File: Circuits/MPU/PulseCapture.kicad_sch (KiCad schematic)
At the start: 12 parts, among them U15 AD7984BRMZ, U18 LT1715

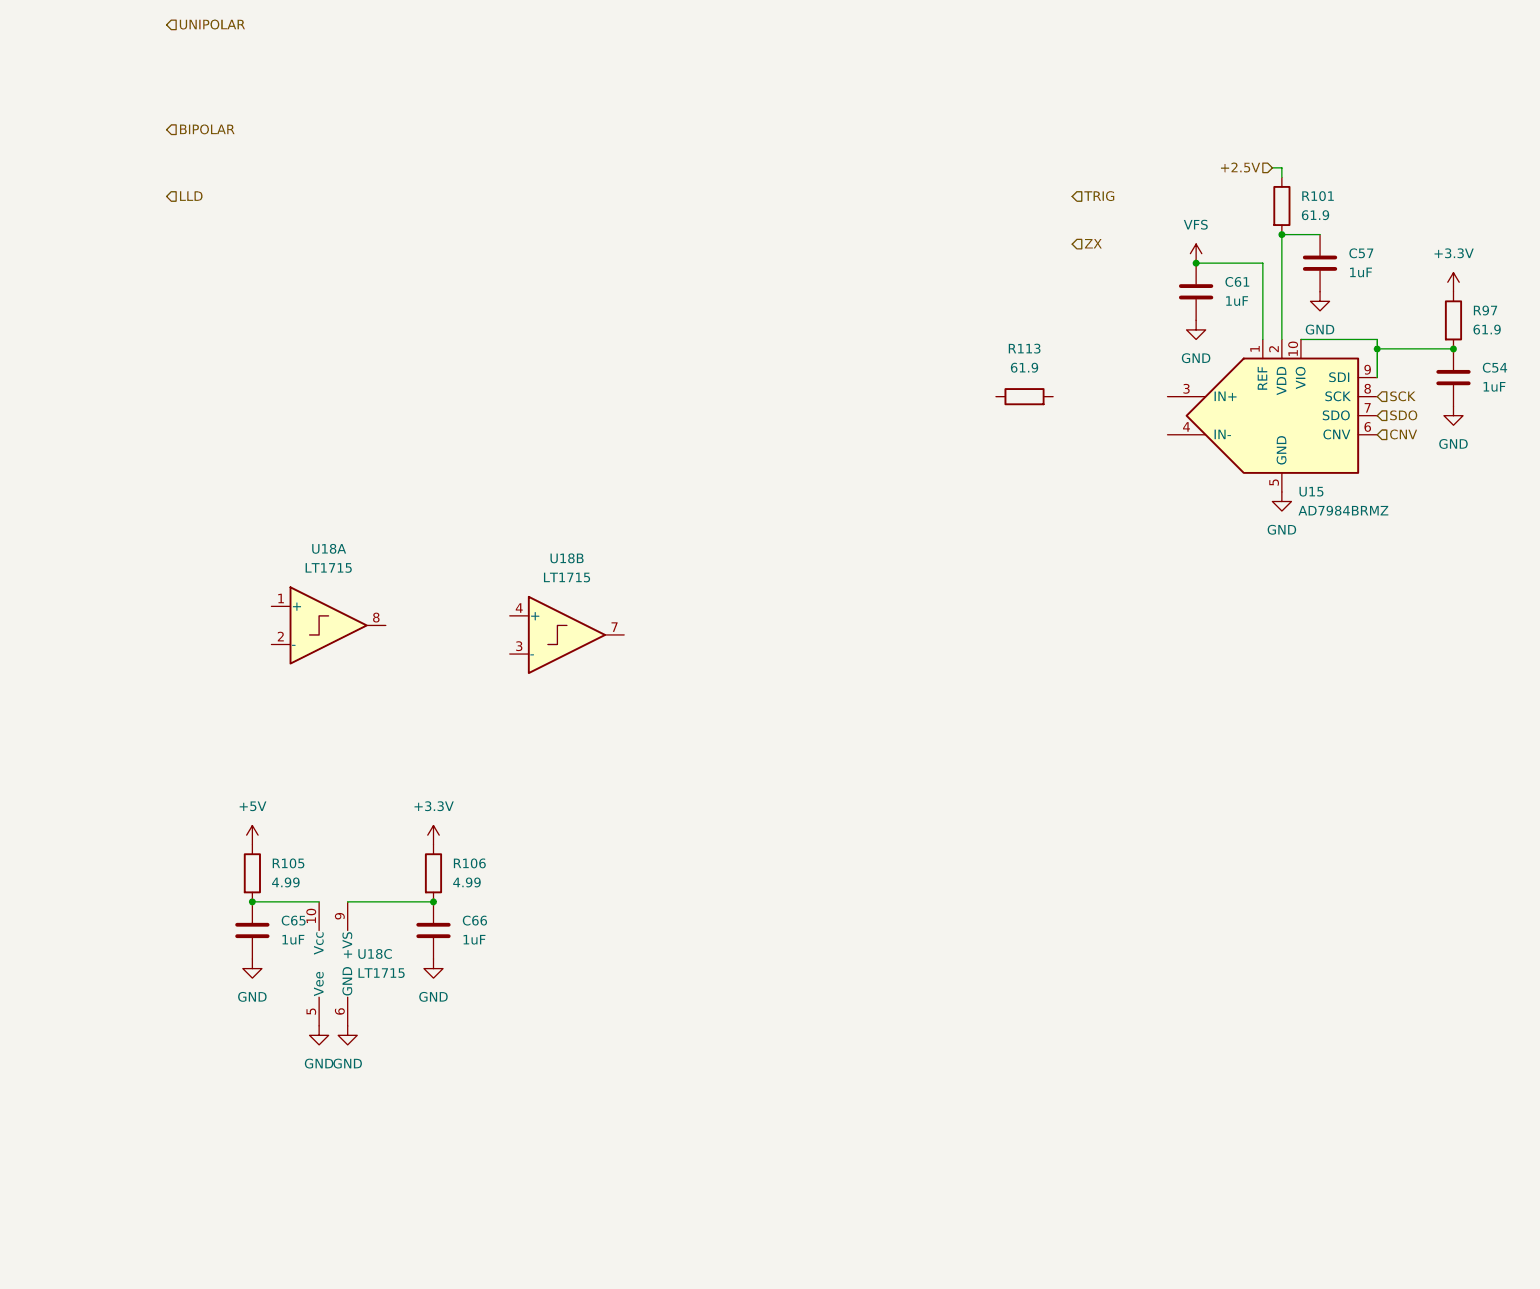
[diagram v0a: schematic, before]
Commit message: All pages populated with parts
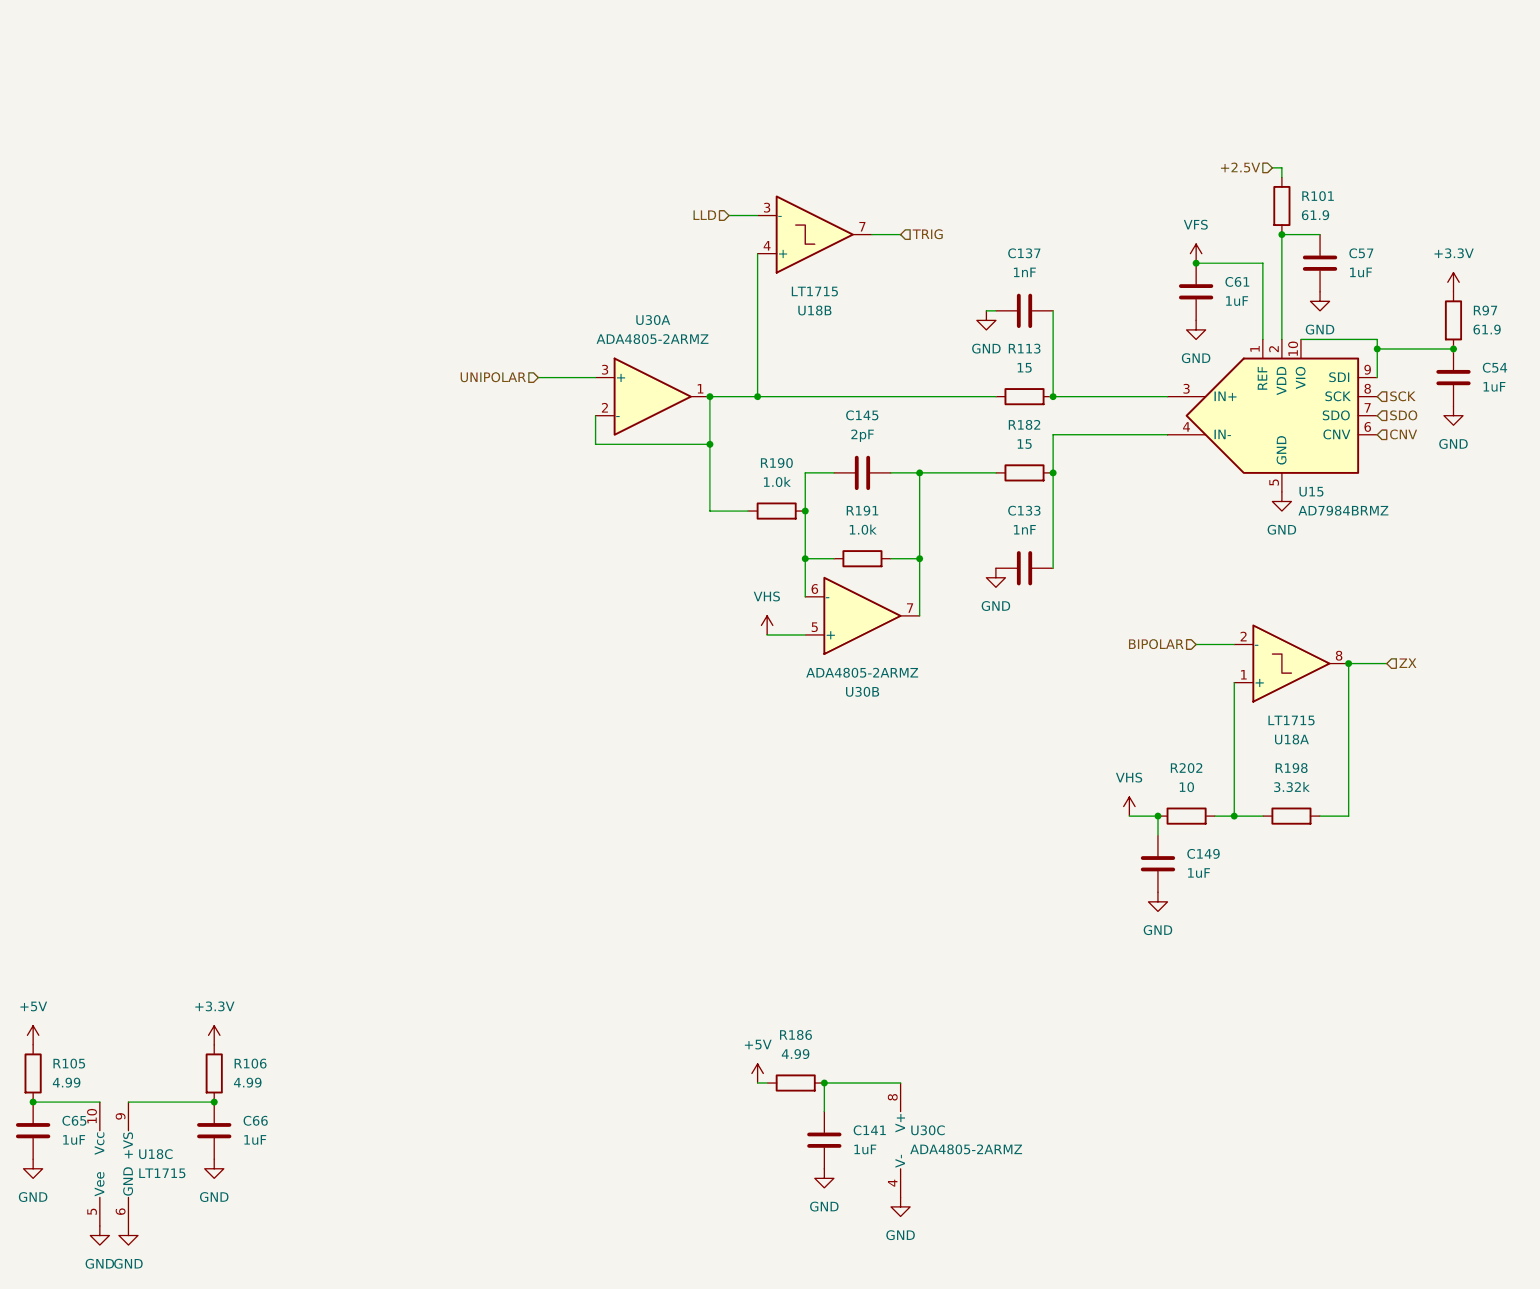
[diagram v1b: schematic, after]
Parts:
- added C133, C137: 1nF, Capacitor_SMD:C_0603_1608Metric, symbol QuERI_symbols:Csmall
- added C141, C149: 1uF, Capacitor_SMD:C_0805_2012Metric, symbol QuERI_symbols:C
- added C145: 2pF, Capacitor_SMD:C_0603_1608Metric, symbol QuERI_symbols:Csmall
- added R182: 15, Resistor_SMD:R_0603_1608Metric, symbol QuERI_symbols:Rlowp
- added R186: 4.99, Resistor_SMD:R_0603_1608Metric, symbol QuERI_symbols:Rlowp
- added R190, R191: 1.0k, Resistor_SMD:R_0603_1608Metric, symbol QuERI_symbols:Rlowp
- added R198: 3.32k, Resistor_SMD:R_0603_1608Metric, symbol QuERI_symbols:Rlowp
- added R202: 10, Resistor_SMD:R_0603_1608Metric, symbol QuERI_symbols:Rlowp
- added U30: ADA4805-2ARMZ, Package_SO:MSOP-8_3x3mm_P0.65mm, symbol QuERI_symbols:ADA4805-2ARMZ
- R113: value 61.9 -> 15
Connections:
- net +5V: now also R186.1
- net BIPOLAR: now also U18.2 (-)
- net GND: now also C133.1, C137.1, C141.2, C149.2, U30.4 (V-)
- net LLD: now also U18.3 (-)
- net TRIG: now also U18.7
- net UNIPOLAR: now also U30.3 (+)
- net ZX: now also U18.8, R198.2
- net at R113.1: now also U18.4 (+), R190.1, U30.1, U30.2 (-)
- net at R113.2: now also U15.3 (IN+), C137.2
- net at U18.1 (+): now also R198.1, R202.2
- net at U15.4 (IN-): now also C133.2, R182.2
- new net: C145.1, R190.2, R191.1, U30.6 (-)
- new net: C145.2, R182.1, R191.2, U30.7
- new net: C141.1, R186.2, U30.8 (V+)
- new net VHS: C149.1, R202.1, U30.5 (+)
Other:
- moved on the sheet: C65, C66, R105, R106, U18A, U18B, U18C

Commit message: Passes DRC
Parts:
- renumbered C65 to C115, C66 to C116, C141 to C117, C145 to C118, C137 to C119, C133 to C120, C149 to C121, C61 to C122, C57 to C123, C54 to C134, R105 to R159, R106 to R160, R190 to R161, R186 to R162, R191 to R163, R113 to R164, R182 to R165, R202 to R166, R101 to R167, R198 to R168, R97 to R169, U18 to U26, U30 to U27, U15 to U31
